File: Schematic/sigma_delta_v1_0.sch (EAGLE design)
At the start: 65 parts, among them IC1 LM50, IC2 MC78M12CDTG, IC3 UA78M33DCY, IC4 LM50, IC5 ACPL-064L-000E, J1 SJ1-3523N, Q3 IRF3707S, Q4 IRF3707S, Q5 BSD223P, X1 1751251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

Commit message: continued routing and added ferrit bead datasheet
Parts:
- BEAD: value TBD -> MMZ0603S102HT000
- renumbered L2 to BEAD
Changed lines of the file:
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@@
 <part name="AVCC_FPGA" library="supply1" deviceset="VCC" device="" value="AVCC_FPGA"/>
 <part name="AGND_FPGA3" library="supply2" deviceset="GND" device="" value="AGND_FPGA"/>
-<part name="L2" library="rcl" deviceset="L-EU" device="L2012C" value="TBD"/>
+<part name="BEAD" library="rcl" deviceset="L-EU" device="L2012C" value="MMZ0603S102HT000"/>
 </parts>
 <sheets>
@@
 <instance part="AVCC_FPGA" gate="VCC" x="58.42" y="66.04"/>
 <instance part="AGND_FPGA3" gate="GND" x="58.42" y="43.18"/>
-<instance part="L2" gate="G$1" x="40.64" y="48.26" rot="R90"/>
+<instance part="BEAD" gate="G$1" x="40.64" y="48.26" rot="R90"/>
 </instances>
 <busses>
@@
 <wire x1="30.48" y1="48.26" x2="30.48" y2="50.8" width="0.1524" layer="91"/>
 <junction x="25.4" y="48.26"/>
-<pinref part="L2" gate="G$1" pin="1"/>
+<pinref part="BEAD" gate="G$1" pin="1"/>
 <wire x1="35.56" y1="48.26" x2="30.48" y2="48.26" width="0.1524" layer="91"/>
 <junction x="30.48" y="48.26"/>
@@
 <junction x="58.42" y="48.26"/>
 <pinref part="AGND_FPGA3" gate="GND" pin="GND"/>
-<pinref part="L2" gate="G$1" pin="2"/>
+<pinref part="BEAD" gate="G$1" pin="2"/>
 <wire x1="45.72" y1="48.26" x2="50.8" y2="48.26" width="0.1524" layer="91"/>
 <junction x="50.8" y="48.26"/>

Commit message: added FPGA_GND polygon to the top layer
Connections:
- net GND: no longer BEAD.1, C17.2, C18.2
- net GND_FPGA: now also BEAD.1, C17.2, C18.2
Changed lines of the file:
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@@
 </variantdefs>
 <classes>
-<class number="0" name="default" width="0" drill="0">
+<class number="0" name="default" width="0.1524" drill="0.3048">
+<clearance class="0" value="0.1524"/>
+</class>
+<class number="1" name="FPGA_Domain" width="0.1524" drill="0.3048">
+<clearance class="1" value="0.1524"/>
 </class>
 </classes>
@@
 <part name="C17" library="rcl" deviceset="C-EU" device="C0603" value="0.1µ"/>
 <part name="C18" library="rcl" deviceset="C-EU" device="C0603" value="1µ"/>
-<part name="SUPPLY5" library="supply2" deviceset="GND" device="" value="F_GND"/>
+<part name="SUPPLY5" library="supply2" deviceset="GND" device="" value="GND_FPGA"/>
 <part name="VCC_FPGA3" library="supply1" deviceset="VCC" device="" value="VCC_FPGA"/>
 <part name="AVCC_FPGA" library="supply1" deviceset="VCC" device="" value="AVCC_FPGA"/>
@@
 </segment>
 </net>
-<net name="N$2" class="0">
+<net name="N$2" class="1">
 <segment>
 <wire x1="66.04" y1="180.34" x2="66.04" y2="152.4" width="0.1524" layer="91"/>
@@
 </segment>
 </net>
-<net name="N$5" class="0">
+<net name="N$5" class="1">
 <segment>
 <pinref part="R1" gate="G$1" pin="1"/>
@@
 </segment>
 </net>
-<net name="N$6" class="0">
+<net name="N$6" class="1">
 <segment>
 <wire x1="88.9" y1="132.08" x2="116.84" y2="132.08" width="0.1524" layer="91"/>
@@
 </segment>
 </net>
-<net name="VCC_FPGA" class="0">
+<net name="VCC_FPGA" class="1">
 <segment>
 <pinref part="R1" gate="G$1" pin="2"/>
@@
 </segment>
 </net>
-<net name="N$29" class="0">
+<net name="N$29" class="1">
 <segment>
 <pinref part="C14" gate="G$1" pin="1"/>
@@
 </segment>
 </net>
-<net name="N$28" class="0">
+<net name="N$28" class="1">
 <segment>
 <pinref part="C13" gate="G$1" pin="1"/>
@@
 <wire x1="139.7" y1="154.94" x2="142.24" y2="154.94" width="0.1524" layer="91"/>
 </segment>
+</net>
+<net name="GND_FPGA" class="0">
+<segment>
+<wire x1="63.5" y1="149.86" x2="60.96" y2="149.86" width="0.1524" layer="91"/>
+<wire x1="60.96" y1="149.86" x2="60.96" y2="147.32" width="0.1524" layer="91"/>
+<pinref part="GND_FPGA" gate="GND" pin="GND"/>
+<wire x1="63.5" y1="149.86" x2="63.5" y2="170.18" width="0.1524" layer="91"/>
+<wire x1="60.96" y1="149.86" x2="50.8" y2="149.86" width="0.1524" layer="91"/>
+<junction x="60.96" y="149.86"/>
+<pinref part="JP1" gate="A" pin="6"/>
+<pinref part="X4" gate="-6" pin="K"/>
+<wire x1="27.94" y1="170.18" x2="63.5" y2="170.18" width="0.1524" layer="91"/>
+</segment>
+<segment>
+<wire x1="106.68" y1="152.4" x2="106.68" y2="154.94" width="0.1524" layer="91"/>
+<pinref part="GND_FPGA1" gate="GND" pin="GND"/>
+<pinref part="R12" gate="G$1" pin="2"/>
+<wire x1="106.68" y1="154.94" x2="106.68" y2="160.02" width="0.1524" layer="91"/>
+<wire x1="104.14" y1="154.94" x2="106.68" y2="154.94" width="0.1524" layer="91"/>
+<junction x="106.68" y="154.94"/>
+<pinref part="U$4" gate="G$1" pin="S"/>
+</segment>
+<segment>
+<wire x1="106.68" y1="114.3" x2="106.68" y2="116.84" width="0.1524" layer="91"/>
+<pinref part="GND_FPGA2" gate="GND" pin="GND"/>
+<pinref part="R11" gate="G$1" pin="2"/>
+<wire x1="106.68" y1="116.84" x2="106.68" y2="119.38" width="0.1524" layer="91"/>
+<wire x1="104.14" y1="116.84" x2="106.68" y2="116.84" width="0.1524" layer="91"/>
+<junction x="106.68" y="116.84"/>
+<pinref part="U$4" gate="G$2" pin="S"/>
+</segment>
 <segment>
 <pinref part="SUPPLY5" gate="GND" pin="GND"/>
@@
 </segment>
 </net>
-<net name="GND_FPGA" class="0">
-<segment>
-<wire x1="63.5" y1="149.86" x2="60.96" y2="149.86" width="0.1524" layer="91"/>
-<wire x1="60.96" y1="149.86" x2="60.96" y2="147.32" width="0.1524" layer="91"/>
-<pinref part="GND_FPGA" gate="GND" pin="GND"/>
-<wire x1="63.5" y1="149.86" x2="63.5" y2="170.18" width="0.1524" layer="91"/>
-<wire x1="60.96" y1="149.86" x2="50.8" y2="149.86" width="0.1524" layer="91"/>
-<junction x="60.96" y="149.86"/>
-<pinref part="JP1" gate="A" pin="6"/>
-<pinref part="X4" gate="-6" pin="K"/>
-<wire x1="27.94" y1="170.18" x2="63.5" y2="170.18" width="0.1524" layer="91"/>
-</segment>
-<segment>
-<wire x1="106.68" y1="152.4" x2="106.68" y2="154.94" width="0.1524" layer="91"/>
-<pinref part="GND_FPGA1" gate="GND" pin="GND"/>
-<pinref part="R12" gate="G$1" pin="2"/>
-<wire x1="106.68" y1="154.94" x2="106.68" y2="160.02" width="0.1524" layer="91"/>
-<wire x1="104.14" y1="154.94" x2="106.68" y2="154.94" width="0.1524" layer="91"/>
-<junction x="106.68" y="154.94"/>
-<pinref part="U$4" gate="G$1" pin="S"/>
-</segment>
-<segment>
-<wire x1="106.68" y1="114.3" x2="106.68" y2="116.84" width="0.1524" layer="91"/>
-<pinref part="GND_FPGA2" gate="GND" pin="GND"/>
-<pinref part="R11" gate="G$1" pin="2"/>
-<wire x1="106.68" y1="116.84" x2="106.68" y2="119.38" width="0.1524" layer="91"/>
-<wire x1="104.14" y1="116.84" x2="106.68" y2="116.84" width="0.1524" layer="91"/>
-<junction x="106.68" y="116.84"/>
-<pinref part="U$4" gate="G$2" pin="S"/>
-</segment>
-</net>
-<net name="AVCC_FPGA" class="0">
+<net name="AVCC_FPGA" class="1">
 <segment>
 <pinref part="C15" gate="G$1" pin="1"/>
@@
 </segment>
 </net>
-<net name="AGND_FPGA" class="0">
+<net name="AGND_FPGA" class="1">
 <segment>
 <pinref part="C16" gate="G$1" pin="2"/>

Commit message: Finished layouting. DRC pending
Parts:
- removed JUMPER1, JUMPER2: 0, resistor:R-EU_R0402
- added SJ2: (no value), jumper:SJ2W
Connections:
- net N$10: now also C5.1, L1.2, SJ2.2, X2-2.K; no longer J1.RING, JUMPER2.1
- net N$24: now also J1.RING, SJ2.3; no longer C5.1, JUMPER1.2, JUMPER2.2, L1.2, X2-2.K
- net N$25: now also SJ2.1; no longer JUMPER1.1
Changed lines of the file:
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@@
 <part name="J1" library="SamacSys_Parts" deviceset="SJ1-3523N" device=""/>
 <part name="VCC_MID2" library="supply1" deviceset="VCC" device="" value="VCC_MID"/>
-<part name="JUMPER2" library="resistor" deviceset="R-EU_" device="R0402" value="0"/>
-<part name="JUMPER1" library="resistor" deviceset="R-EU_" device="R0402" value="0"/>
 <part name="U$4" library="SamacSys_Parts" deviceset="BSD235N" device=""/>
 <part name="VCC_MID3" library="supply1" deviceset="VCC" device="" value="VCC_MID"/>
@@
 <part name="AGND_FPGA3" library="supply2" deviceset="GND" device="" value="AGND_FPGA"/>
 <part name="BEAD" library="rcl" deviceset="L-EU" device="L2012C" value="MMZ0603S102HT000"/>
+<part name="SJ2" library="jumper" deviceset="SJ2W" device=""/>
 </parts>
 <sheets>
@@
 <instance part="J1" gate="G$1" x="259.08" y="187.96"/>
 <instance part="VCC_MID2" gate="VCC" x="256.54" y="198.12"/>
-<instance part="JUMPER2" gate="G$1" x="302.26" y="187.96"/>
-<instance part="JUMPER1" gate="G$1" x="302.26" y="180.34"/>
 <instance part="U$4" gate="G$1" x="106.68" y="165.1"/>
 <instance part="U$4" gate="G$2" x="106.68" y="124.46"/>
@@
 <instance part="AGND_FPGA3" gate="GND" x="58.42" y="43.18"/>
 <instance part="BEAD" gate="G$1" x="40.64" y="48.26" rot="R90"/>
+<instance part="SJ2" gate="G$1" x="304.8" y="182.88" rot="R180"/>
 </instances>
 <busses>
@@
 </segment>
 </net>
-<net name="N$24" class="0">
+<net name="N$10" class="0">
 <segment>
 <pinref part="L1" gate="G$1" pin="2"/>
@@
 <wire x1="314.96" y1="144.78" x2="309.88" y2="144.78" width="0.1524" layer="91"/>
 <junction x="314.96" y="144.78"/>
-<pinref part="JUMPER2" gate="G$1" pin="2"/>
-<wire x1="309.88" y1="144.78" x2="309.88" y2="180.34" width="0.1524" layer="91"/>
-<wire x1="309.88" y1="180.34" x2="309.88" y2="187.96" width="0.1524" layer="91"/>
-<wire x1="309.88" y1="187.96" x2="307.34" y2="187.96" width="0.1524" layer="91"/>
-<pinref part="JUMPER1" gate="G$1" pin="2"/>
-<wire x1="307.34" y1="180.34" x2="309.88" y2="180.34" width="0.1524" layer="91"/>
-<junction x="309.88" y="180.34"/>
-</segment>
-</net>
-<net name="N$10" class="0">
-<segment>
-<pinref part="J1" gate="G$1" pin="RING"/>
-<wire x1="297.18" y1="187.96" x2="294.64" y2="187.96" width="0.1524" layer="91"/>
-<pinref part="JUMPER2" gate="G$1" pin="1"/>
-</segment>
-</net>
-<net name="N$25" class="0">
-<segment>
-<pinref part="JUMPER1" gate="G$1" pin="1"/>
-<pinref part="J1" gate="G$1" pin="TIP"/>
-<wire x1="294.64" y1="180.34" x2="297.18" y2="180.34" width="0.1524" layer="91"/>
+<wire x1="309.88" y1="144.78" x2="309.88" y2="182.88" width="0.1524" layer="91"/>
+<pinref part="SJ2" gate="G$1" pin="2"/>
 </segment>
 </net>
@@
 </segment>
 </net>
+<net name="N$24" class="0">
+<segment>
+<pinref part="SJ2" gate="G$1" pin="3"/>
+<pinref part="J1" gate="G$1" pin="RING"/>
+<wire x1="294.64" y1="187.96" x2="304.8" y2="187.96" width="0.1524" layer="91"/>
+</segment>
+</net>
+<net name="N$25" class="0">
+<segment>
+<pinref part="J1" gate="G$1" pin="TIP"/>
+<wire x1="294.64" y1="180.34" x2="297.18" y2="180.34" width="0.1524" layer="91"/>
+<pinref part="SJ2" gate="G$1" pin="1"/>
+<wire x1="304.8" y1="177.8" x2="297.18" y2="177.8" width="0.1524" layer="91"/>
+<wire x1="297.18" y1="177.8" x2="297.18" y2="180.34" width="0.1524" layer="91"/>
+</segment>
+</net>

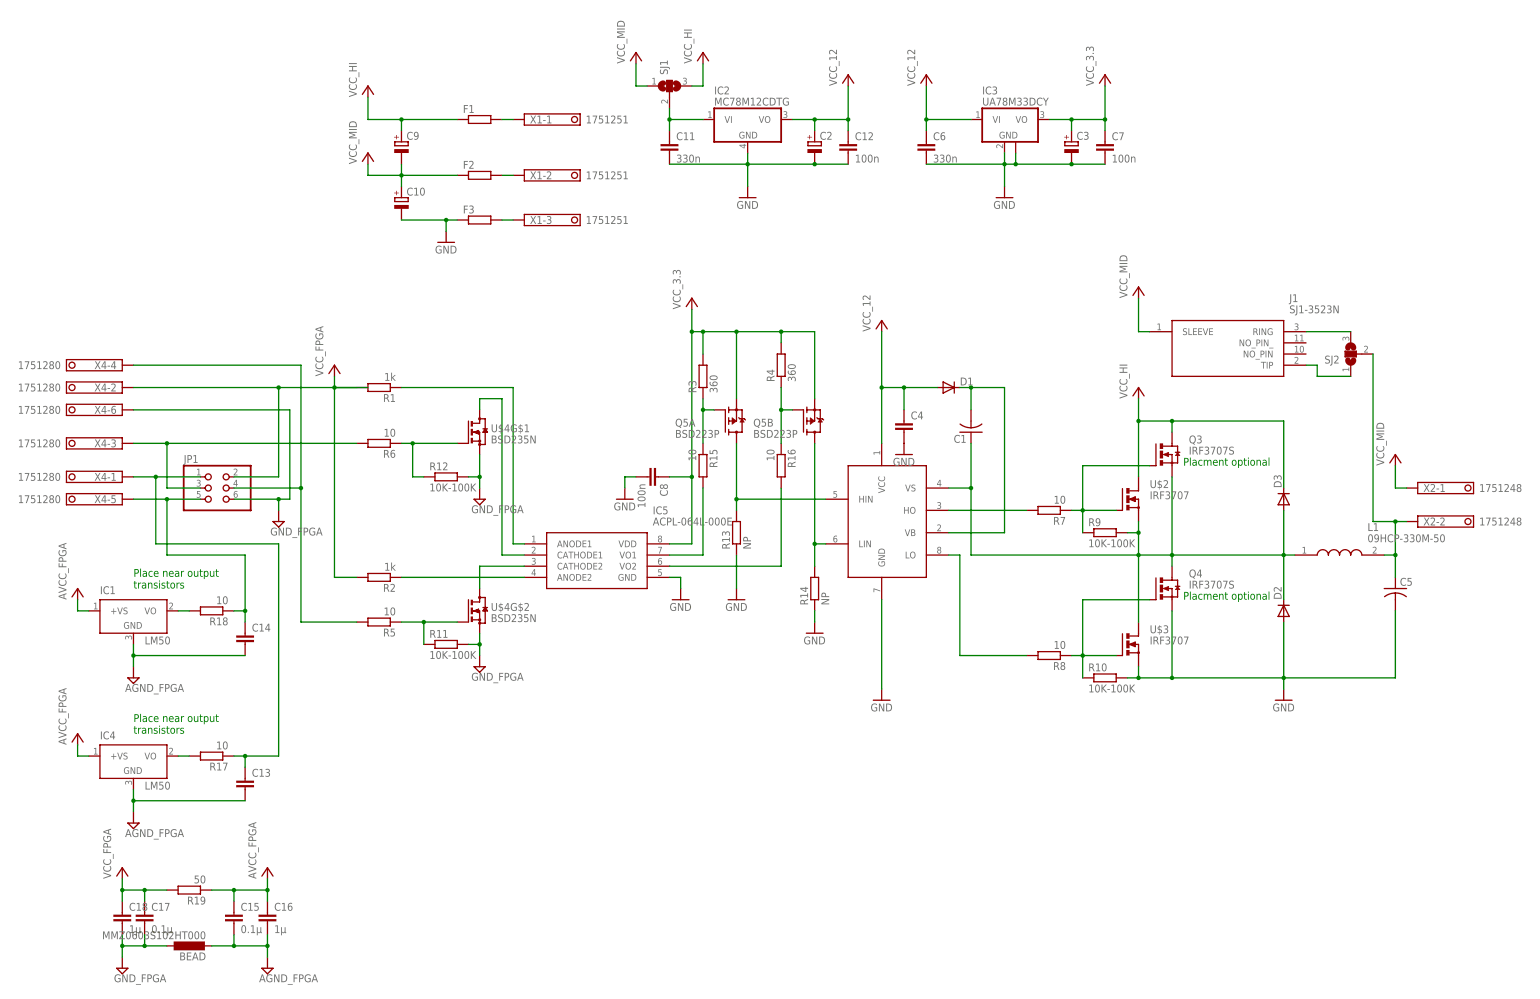
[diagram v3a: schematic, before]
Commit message: adapted wireing width of power stage and exchanged bootstrap capacitor
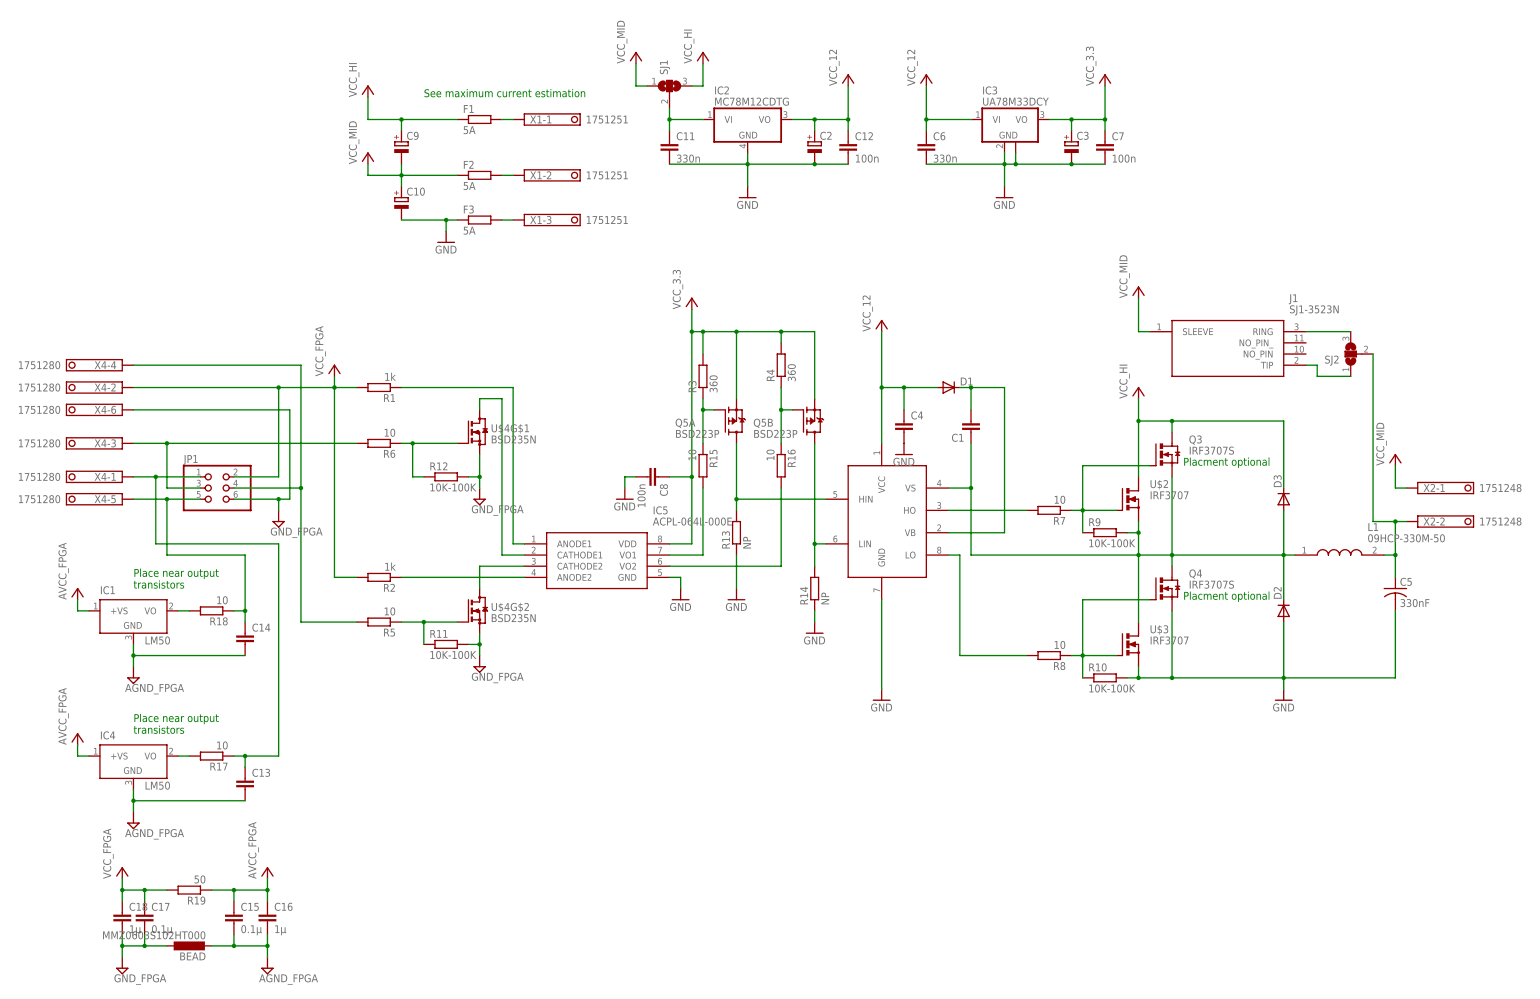
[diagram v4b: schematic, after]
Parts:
- C1: device rcl:C-USC2220K -> rcl:C-EUC0805K
- C5: value (none) -> 330nF
- F1, F2, F3: value (none) -> 5A
- SJ2: device jumper:SJ2W -> jumper:SJ2WW
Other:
- note added: "See maximum current estimation"
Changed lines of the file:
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@@
 <setting verticaltext="up"/>
 </settings>
-<grid distance="0.1" unitdist="inch" unit="inch" style="lines" multiple="1" display="no" altdistance="0.01" altunitdist="inch" altunit="inch"/>
+<grid distance="0.1" unitdist="inch" unit="inch" style="lines" multiple="1" display="yes" altdistance="0.01" altunitdist="inch" altunit="inch"/>
 <layers>
 <layer number="1" name="Top" color="4" fill="1" visible="no" active="no"/>
@@
 <part name="GND_FPGA" library="supply2" deviceset="GND" device="" value="GND_FPGA"/>
 <part name="GND1" library="supply1" deviceset="GND" device=""/>
-<part name="C1" library="rcl" deviceset="C-US" device="C2220K"/>
+<part name="C1" library="rcl" deviceset="C-EU" device="C0805K"/>
 <part name="C2" library="rcl" deviceset="CPOL-EU" device="UD-6,3X7,7"/>
 <part name="U$3" library="transistor-power" deviceset="BUZ11" device="BV" value="IRF3707"/>
@@
 <part name="U$1" library="IR2011" deviceset="IR2011" device=""/>
 <part name="L1" library="SamacSys_Parts" deviceset="09HCP-330M-50" device=""/>
-<part name="C5" library="rcl" deviceset="C-US" device="C2220K"/>
+<part name="C5" library="rcl" deviceset="C-US" device="C2220K" value="330nF"/>
 <part name="D2" library="diode" deviceset="DIODE-" device="DO214AC"/>
 <part name="D3" library="diode" deviceset="DIODE-" device="DO214AC"/>
 <part name="GND4" library="supply1" deviceset="GND" device=""/>
-<part name="F1" library="rcl" deviceset="R-EU_" device="M1206"/>
-<part name="F2" library="rcl" deviceset="R-EU_" device="M1206"/>
+<part name="F1" library="rcl" deviceset="R-EU_" device="M1206" value="5A"/>
+<part name="F2" library="rcl" deviceset="R-EU_" device="M1206" value="5A"/>
 <part name="X1" library="con-phoenix-350" deviceset="1751251" device=""/>
 <part name="GND7" library="supply1" deviceset="GND" device=""/>
@@
 </part>
 <part name="U$2" library="transistor-power" deviceset="BUZ11" device="BV" value="IRF3707"/>
-<part name="F3" library="rcl" deviceset="R-EU_" device="M1206"/>
+<part name="F3" library="rcl" deviceset="R-EU_" device="M1206" value="5A"/>
 <part name="J1" library="SamacSys_Parts" deviceset="SJ1-3523N" device=""/>
 <part name="VCC_MID2" library="supply1" deviceset="VCC" device="" value="VCC_MID"/>
@@
 <part name="AGND_FPGA3" library="supply2" deviceset="GND" device="" value="AGND_FPGA"/>
 <part name="BEAD" library="rcl" deviceset="L-EU" device="L2012C" value="MMZ0603S102HT000"/>
-<part name="SJ2" library="jumper" deviceset="SJ2W" device=""/>
+<part name="SJ2" library="jumper" deviceset="SJ2W" device="W"/>
 </parts>
 <sheets>
@@
 <text x="27.94" y="96.52" size="1.778" layer="91">Place near output
 transistors</text>
+<text x="93.98" y="241.3" size="1.778" layer="91">See maximum current estimation</text>
 </plain>
 <instances>
@@
 <junction x="73.66" y="175.26"/>
 <wire x1="60.96" y1="175.26" x2="73.66" y2="175.26" width="0.1524" layer="91"/>
-<wire x1="73.66" y1="175.26" x2="81.28" y2="175.26" width="0.1524" layer="91"/>
 <pinref part="VCC_FPGA" gate="VCC" pin="VCC"/>
 <wire x1="73.66" y1="175.26" x2="73.66" y2="177.8" width="0.1524" layer="91"/>
@@
 </sheet>
 </sheets>
+<errors>
+</errors>
 </schematic>
 </drawing>

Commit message: ERC and DRC done. Ready for production.
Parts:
- C1: value (none) -> 4.7µ
- C4: value (none) -> 100n
